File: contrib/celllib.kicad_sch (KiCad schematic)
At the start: 110 parts, among them Q1 PMOS, Q10 NMOS, Q100 PMOS, Q101 PMOS, Q102 PMOS, Q11 PMOS, Q12 NMOS, Q13 PMOS, Q14 NMOS, Q15 PMOS, Q16 PMOS, Q17 PMOS, Q18 NMOS, Q19 NMOS, Q2 PMOS, Q20 PMOS, Q21 PMOS, Q22 NMOS, Q23 NMOS, Q24 PMOS, Q25 PMOS, Q26 NMOS, Q27 NMOS, Q28 PMOS, Q29 NMOS, Q3 NMOS, Q30 PMOS, Q31 PMOS, Q32 PMOS, Q33 NMOS, Q34 NMOS, Q35 NMOS, Q36 PMOS, Q37 NMOS, Q38 PMOS, Q39 PMOS, Q4 PMOS, Q40 NMOS, Q41 NMOS, Q42 PMOS, Q43 NMOS, Q44 PMOS, Q45 PMOS, Q46 PMOS, Q47 NMOS, Q48 NMOS, Q49 NMOS, Q5 PMOS, Q50 PMOS, Q51 NMOS, Q52 PMOS, Q53 PMOS, Q54 PMOS, Q55 NMOS, Q56 NMOS, Q57 PMOS, Q58 PMOS, Q59 NMOS, Q6 NMOS, Q60 PMOS, Q61 NMOS, Q62 PMOS, Q63 NMOS, Q64 PMOS, Q65 NMOS, Q66 NMOS, Q67 PMOS, Q68 NMOS, Q69 PMOS, Q7 PMOS, Q70 NMOS, Q71 PMOS, Q72 NMOS, Q73 PMOS, Q74 PMOS, Q75 PMOS, Q76 PMOS, Q77 NMOS, Q78 NMOS, Q79 NMOS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

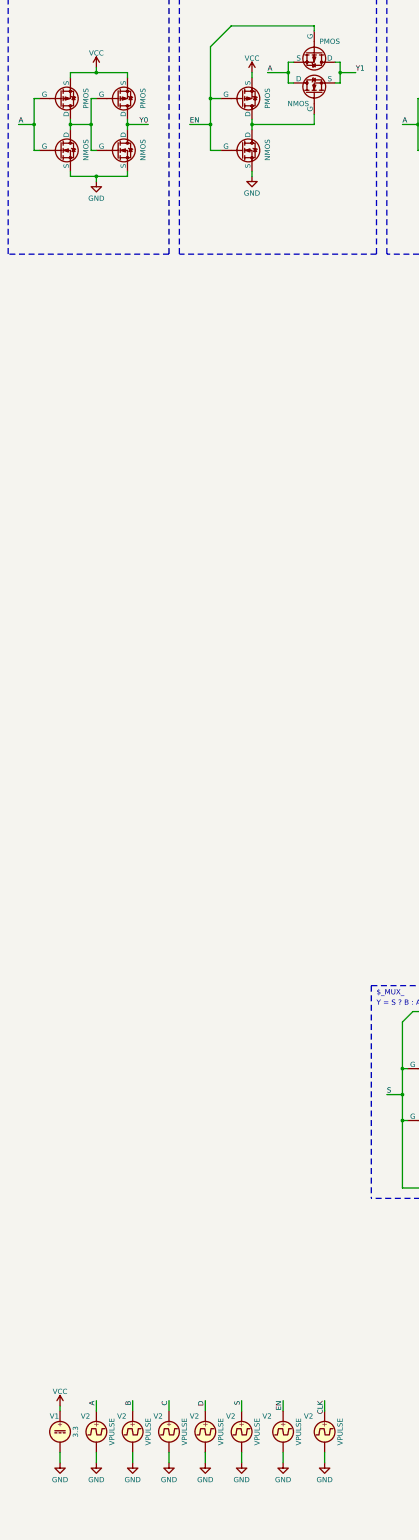
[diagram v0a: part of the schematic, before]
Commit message: Updated some SIM params, the `$_TBUF_` cell is broken, needs fixing
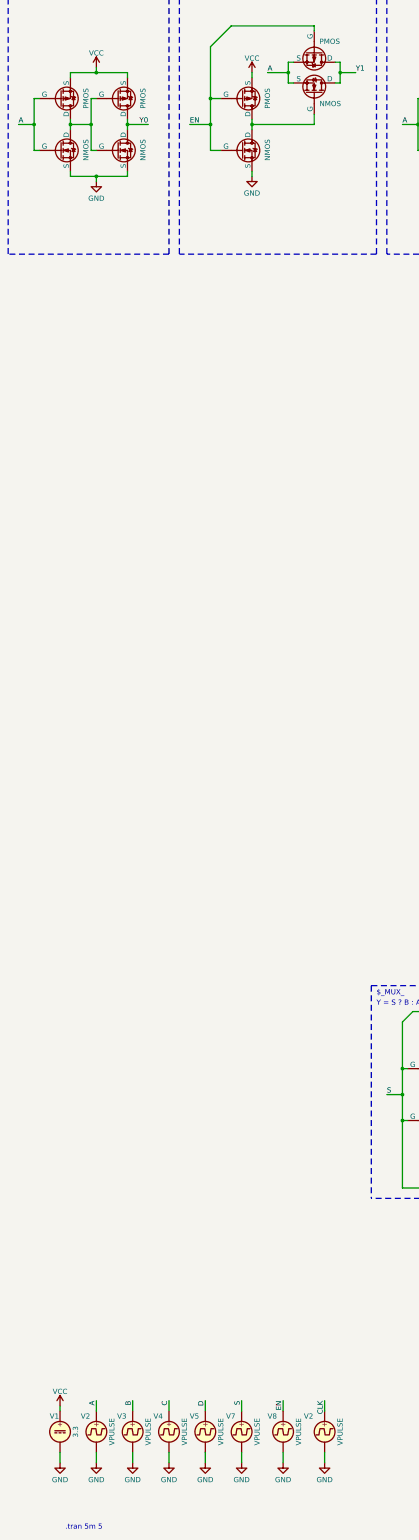
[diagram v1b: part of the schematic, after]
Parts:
- removed V2 (x5): VPULSE, symbol Simulation_SPICE:VPULSE
- added V3, V4, V5, V7, V8: VPULSE, symbol Simulation_SPICE:VPULSE
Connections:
- net A: now also Q56.3 (S); no longer Q56.1 (D)
- net B: now also V3.1
- net C: now also V4.1
- net D: now also V5.1
- net EN: now also V8.1
- net GND: now also V3.2, V4.2, V5.2, V7.2, V8.2
- net S: now also V7.1
- net Y1: now also Q56.1 (D); no longer Q56.3 (S)
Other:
- note added: ".tran 5m 5"
